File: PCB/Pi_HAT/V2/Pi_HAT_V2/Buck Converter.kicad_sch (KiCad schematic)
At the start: 19 parts, among them J5 XT60PW-M, J6 Conn_01x04_Male, U1 MP2315GJ-Z

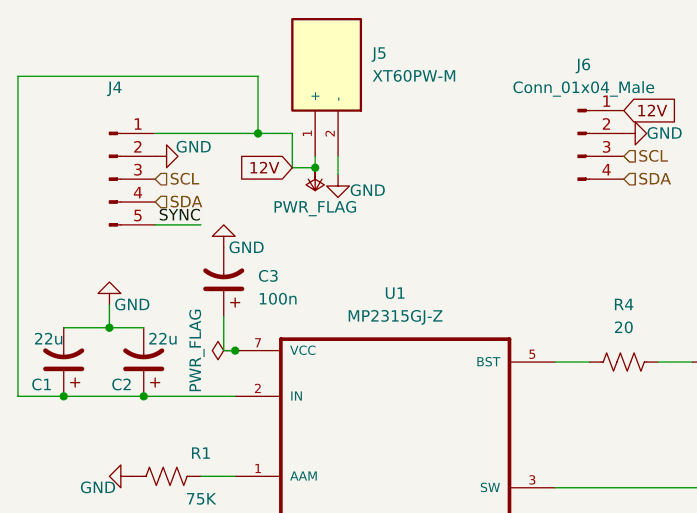
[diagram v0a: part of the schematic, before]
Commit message: Finished Buch .sch
Next need to start/finish the PCB traces
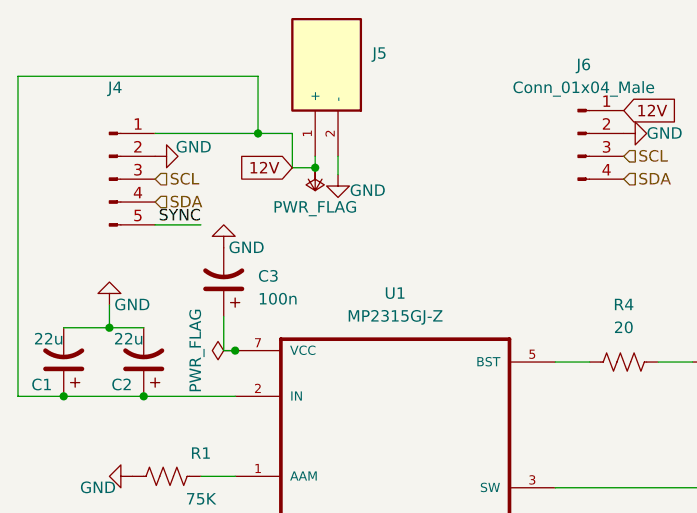
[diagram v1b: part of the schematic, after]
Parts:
- J5: value XT60PW-M -> (none); footprint .pretty:AMASS_XT60PW-M -> (none)
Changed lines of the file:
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@@
       (effects (font (size 1.27 1.27)) (justify right))
     )
-    (property "Value" "XT60PW-M" (id 1) (at 123.19 35.5599 90)
-      (effects (font (size 1.27 1.27)) (justify right))
-    )
-    (property "Footprint" ".pretty:AMASS_XT60PW-M" (id 2) (at 119.38 34.29 0)
+    (property "Value" "" (id 1) (at 123.19 35.5599 90)
+      (effects (font (size 1.27 1.27)) (justify right))
+    )
+    (property "Footprint" "" (id 2) (at 119.38 34.29 0)
       (effects (font (size 1.27 1.27)) (justify left bottom) hide)
     )
@@
       (effects (font (size 1.27 1.27)) hide)
     )
-    (property "Value" "" (id 1) (at 116.84 50.165 0))
+    (property "Value" "~" (id 1) (at 116.84 50.165 0))
     (property "Footprint" "" (id 2) (at 116.84 45.72 0)
       (effects (font (size 1.27 1.27)) hide)
@@
       (effects (font (size 1.27 1.27)) (justify left))
     )
-    (property "Value" "22u" (id 1) (at 101.6 64.77 0)
-      (effects (font (size 1.27 1.27)) (justify left))
-    )
+    (property "Value" "22u" (id 1) (at 97.79 64.77 0)
+      (effects (font (size 1.27 1.27)) (justify left))
+    )

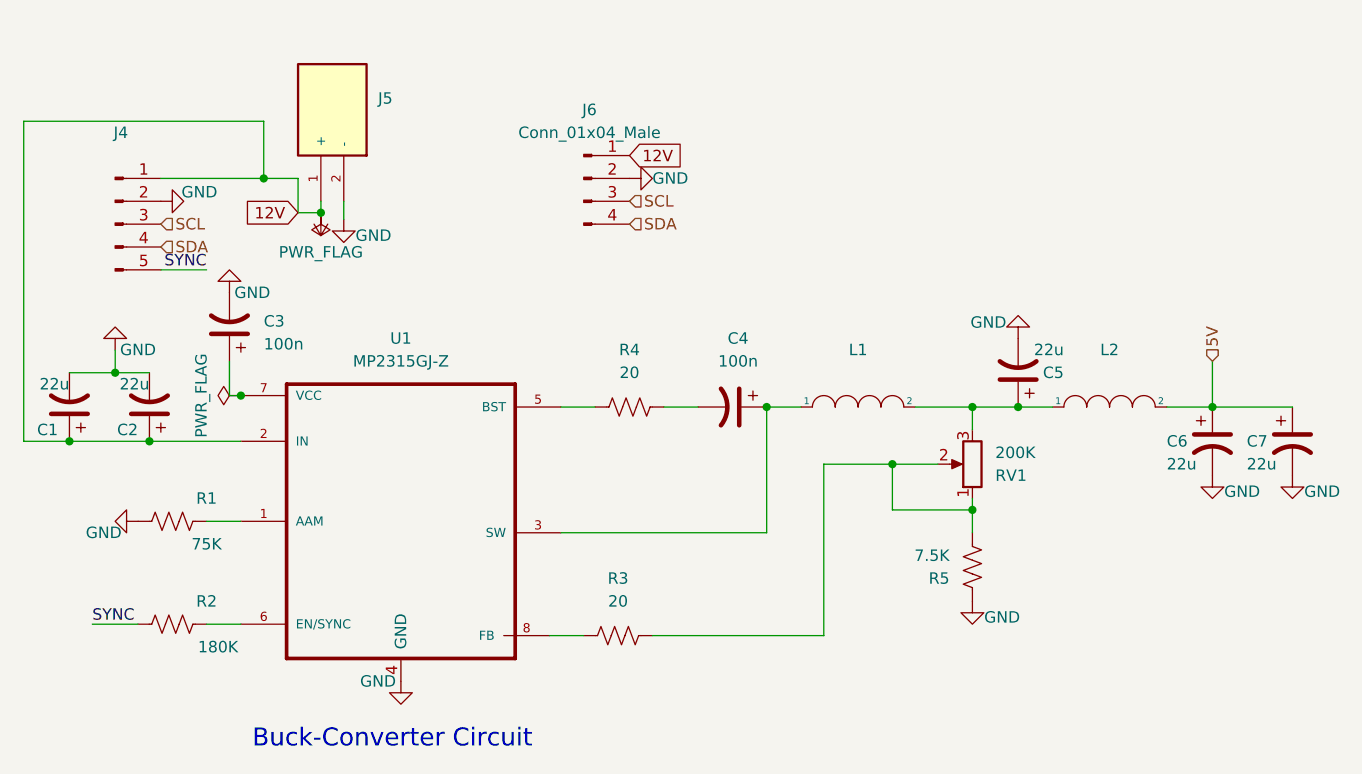
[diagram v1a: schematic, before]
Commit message: Updated
Added NANO_HAT and finished the PI_HAT V2 .sch, need to start/finish traces
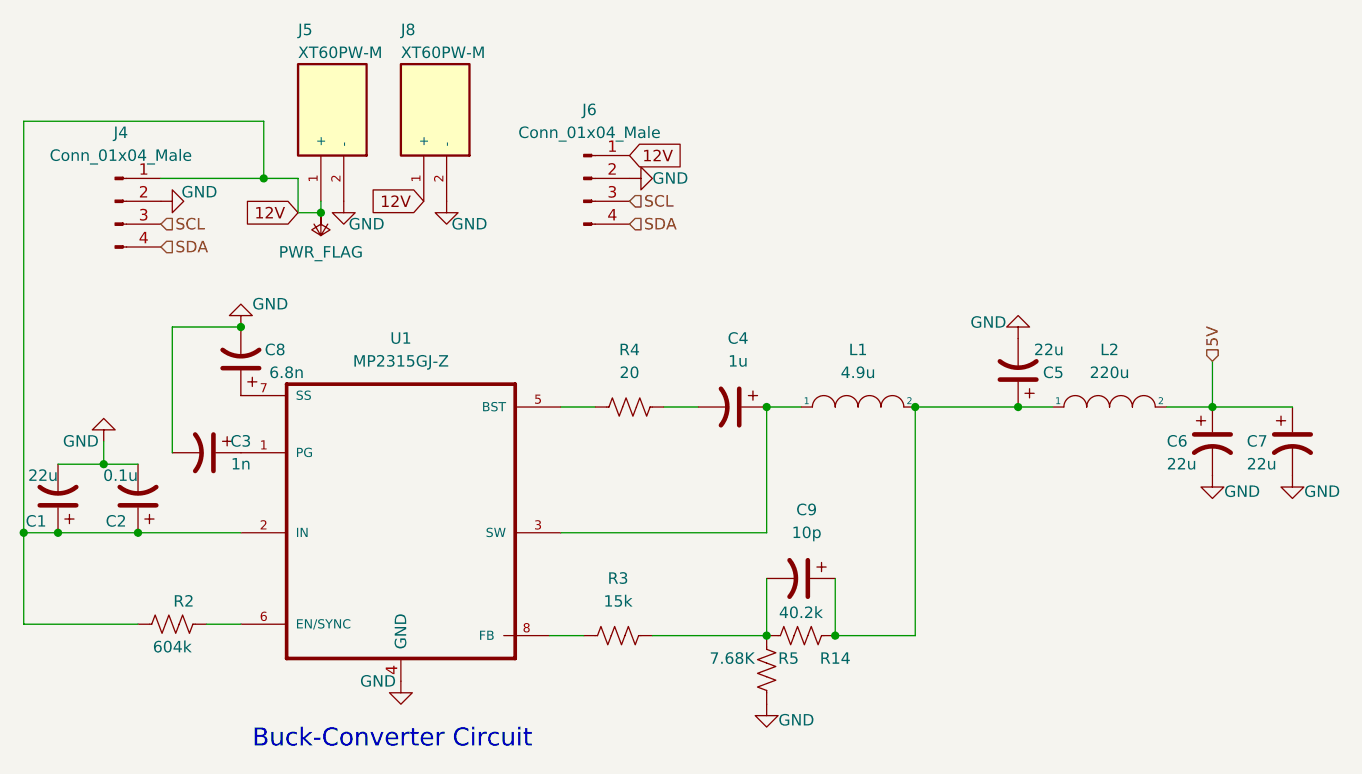
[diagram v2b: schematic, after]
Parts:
- removed J4: (no value), symbol Connector:Conn_01x05_Male
- removed R1: 75K, Resistor_SMD:R_0805_2012Metric_Pad1.20x1.40mm_HandSolder, symbol Device:R_US
- removed RV1: 200K, .pretty:TRIM_3296W-1-204LF, symbol Device:R_Potentiometer
- added C8: 6.8n, Capacitor_SMD:C_0603_1608Metric_Pad1.08x0.95mm_HandSolder, symbol Device:C_Polarized_US
- added C9: 10p, Capacitor_SMD:C_0603_1608Metric_Pad1.08x0.95mm_HandSolder, symbol Device:C_Polarized_US
- added J4: Conn_01x04_Male, Connector_PinHeader_2.54mm:PinHeader_1x04_P2.54mm_Vertical, symbol Connector:Conn_01x04_Male
- added J8: XT60PW-M, .pretty:AMASS_XT60PW-M, symbol XT60PW-M:XT60PW-M
- added R14: 40.2k, Resistor_SMD:R_0805_2012Metric_Pad1.20x1.40mm_HandSolder, symbol Device:R_US
- C2: value 22u -> 0.1u
- C3: value 100n -> 1n; footprint Capacitor_SMD:C_0805_2012Metric_Pad1.18x1.45mm_HandSolder -> Capacitor_SMD:C_0603_1608Metric_Pad1.08x0.95mm_HandSolder
- C4: value 100n -> 1u
- J5: value (none) -> XT60PW-M; footprint (none) -> .pretty:AMASS_XT60PW-M
- J6: footprint (none) -> Connector_PinHeader_2.54mm:PinHeader_1x04_P2.54mm_Vertical
- L1: value (none) -> 4.9u; footprint (none) -> .pretty:744777004; order https://www.digikey.com/en/products/detail/w%C3%BCrth-elekt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 -> https://www.mouser.com/ProductDetail/Coiltronics-Eaton/SD70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
- L2: value (none) -> 220u; footprint (none) -> .pretty:IND_AIRD-02-151K
- R2: value 180K -> 604k
- R3: value 20 -> 15k
- R4: footprint Resistor_SMD:R_0805_2012Metric_Pad1.20x1.40mm_HandSolder -> Resistor_SMD:R_0603_1608Metric_Pad0.98x0.95mm_HandSolder
- R5: value 7.5K -> 7.68K
- U1: footprint .pretty:SOT65P280X100-8N -> .pretty:MP2393GTL-P; Field4 Monolithic Power -> (none); Order (none) -> https://www.mouser.com/ProductDetail/Monolithic-Power-Syste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
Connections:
- net SYNC is gone; now on net +12V: R2.1
- net +12V: now also J4.1 (Pin_1), J8.1 (+)
- net GND: now also C8.2, J4.2 (Pin_2), J8.2 (-)
- net SCL: now also J4.3 (Pin_3)
- net SDA: now also J4.4 (Pin_4)
- net at U1.1 (PG): now also C3.1
- net at U1.7 (SS): now also C8.1; no longer C3.1
- net at R3.2, R5.2: now also C9.2, R14.2
- net at C5.1, L1.2, L2.1: now also C9.1, R14.1
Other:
- moved on the sheet: C1, C2, C3, R5

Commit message: Updated (Gerber)
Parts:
- removed J8: XT60PW-M, .pretty:AMASS_XT60PW-M, symbol XT60PW-M:XT60PW-M
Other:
- moved on the sheet: J6
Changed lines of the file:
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@@
     )
   )
-  (global_label "12V" (shape input) (at 128.27 44.45 180) (fields_autoplaced)
-    (effects (font (size 1.27 1.27)) (justify right))
-    (property "Intersheet References" "${INTERSHEET_REFS}" (id 0) (at 4.318 -2.032 0)
-      (effects (font (size 1.27 1.27)) hide)
-    )
-  )
-  (global_label "12V" (shape input) (at 151.13 39.37 0) (fields_autoplaced)
-    (effects (font (size 1.27 1.27)) (justify left))
-    (property "Intersheet References" "${INTERSHEET_REFS}" (id 0) (at 275.082 85.852 0)
-      (effects (font (size 1.27 1.27)) hide)
-    )
-  )
-  (hierarchical_label "SCL" (shape input) (at 151.13 44.45 0)
+  (global_label "12V" (shape input) (at 137.16 34.544 0) (fields_autoplaced)
+    (effects (font (size 1.27 1.27)) (justify left))
+    (property "Intersheet References" "${INTERSHEET_REFS}" (id 0) (at 261.112 81.026 0)
+      (effects (font (size 1.27 1.27)) hide)
+    )
+  )
+  (hierarchical_label "SCL" (shape input) (at 137.16 39.624 0)
     (effects (font (size 1.27 1.27)) (justify left))
   )
@@
     (effects (font (size 1.27 1.27)) (justify left))
   )
-  (hierarchical_label "SDA" (shape input) (at 151.13 46.99 0)
+  (hierarchical_label "SDA" (shape input) (at 137.16 42.164 0)
     (effects (font (size 1.27 1.27)) (justify left))
   )
@@
     (property "Datasheet" "~" (id 3) (at 224.79 71.12 0)
       (effects (font (size 1.27 1.27)) hide)
-    )
-    (pin "1")
-    (pin "2")
-  )
-  (symbol (lib_id "XT60PW-M:XT60PW-M") (at 130.81 34.29 90) (unit 1)
-    (in_bom yes) (on_board yes)
-    (property "Reference" "J8" (id 0) (at 125.73 25.4 90)
-      (effects (font (size 1.27 1.27)) (justify right))
-    )
-    (property "Value" "XT60PW-M" (id 1) (at 125.73 27.94 90)
-      (effects (font (size 1.27 1.27)) (justify right))
-    )
-    (property "Footprint" ".pretty:AMASS_XT60PW-M" (id 2) (at 130.81 34.29 0)
-      (effects (font (size 1.27 1.27)) (justify left bottom) hide)
-    )
-    (property "Datasheet" "" (id 3) (at 130.81 34.29 0)
-      (effects (font (size 1.27 1.27)) (justify left bottom) hide)
-    )
-    (property "STANDARD" "Manufacturer recommendations" (id 4) (at 130.81 34.29 0)
-      (effects (font (size 1.27 1.27)) (justify left bottom) hide)
-    )
-    (property "PARTREV" "V1.2" (id 5) (at 130.81 34.29 0)
-      (effects (font (size 1.27 1.27)) (justify left bottom) hide)
-    )
-    (property "MANUFACTURER" "AMASS" (id 6) (at 130.81 34.29 0)
-      (effects (font (size 1.27 1.27)) (justify left bottom) hide)
-    )
-    (property "MAXIMUM_PACKAGE_HEIGHT" "8.4 mm" (id 7) (at 130.81 34.29 0)
-      (effects (font (size 1.27 1.27)) (justify left bottom) hide)
     )
     (pin "1")
@@
     (pin "1")
     (pin "2")
-  )
-  (symbol (lib_id "power:GND") (at 130.81 44.45 0) (unit 1)
-    (in_bom yes) (on_board yes)
-    (property "Reference" "#PWR0116" (id 0) (at 130.81 50.8 0)
-      (effects (font (size 1.27 1.27)) hide)
-    )
-    (property "Value" "GND" (id 1) (at 133.35 46.99 0))
-    (property "Footprint" "" (id 2) (at 130.81 44.45 0)
-      (effects (font (size 1.27 1.27)) hide)
-    )
-    (property "Datasheet" "" (id 3) (at 130.81 44.45 0)
-      (effects (font (size 1.27 1.27)) hide)
-    )
-    (pin "1")
   )
   (symbol (lib_id "Device:R_US") (at 151.13 67.31 90) (unit 1)
@@
     (pin "2")
   )
-  (symbol (lib_id "power:GND") (at 151.13 41.91 90) (unit 1)
-    (in_bom yes) (on_board yes)
-    (property "Reference" "#PWR0117" (id 0) (at 157.48 41.91 0)
-      (effects (font (size 1.27 1.27)) hide)
-    )
-    (property "Value" "GND" (id 1) (at 153.67 41.91 90)
-      (effects (font (size 1.27 1.27)) (justify right))
-    )
-    (property "Footprint" "" (id 2) (at 151.13 41.91 0)
-      (effects (font (size 1.27 1.27)) hide)
-    )
-    (property "Datasheet" "" (id 3) (at 151.13 41.91 0)
+  (symbol (lib_id "power:GND") (at 137.16 37.084 90) (unit 1)
+    (in_bom yes) (on_board yes)
+    (property "Reference" "#PWR0117" (id 0) (at 143.51 37.084 0)
+      (effects (font (size 1.27 1.27)) hide)
+    )
+    (property "Value" "GND" (id 1) (at 139.7 37.084 90)
+      (effects (font (size 1.27 1.27)) (justify right))
+    )
+    (property "Footprint" "" (id 2) (at 137.16 37.084 0)
+      (effects (font (size 1.27 1.27)) hide)
+    )
+    (property "Datasheet" "" (id 3) (at 137.16 37.084 0)
       (effects (font (size 1.27 1.27)) hide)
     )
@@
     (pin "2")
   )
-  (symbol (lib_id "Connector:Conn_01x04_Male") (at 146.05 41.91 0) (unit 1)
-    (in_bom yes) (on_board yes) (fields_autoplaced)
-    (property "Reference" "J6" (id 0) (at 146.685 34.29 0))
-    (property "Value" "Conn_01x04_Male" (id 1) (at 146.685 36.83 0))
-    (property "Footprint" "Connector_PinHeader_2.54mm:PinHeader_1x04_P2.54mm_Vertical" (id 2) (at 146.05 41.91 0)
-      (effects (font (size 1.27 1.27)) hide)
-    )
-    (property "Datasheet" "~" (id 3) (at 146.05 41.91 0)
-      (effects (font (size 1.27 1.27)) hide)
-    )
+  (symbol (lib_id "Connector:Conn_01x04_Male") (at 132.08 37.084 0) (unit 1)
+    (in_bom yes) (on_board yes) (fields_autoplaced)
+    (property "Reference" "J6" (id 0) (at 132.715 29.464 0))
+    (property "Value" "Conn_01x04_Male" (id 1) (at 132.715 32.004 0))
+    (property "Footprint" "Connector_PinHeader_2.54mm:PinHeader_1x04_P2.54mm_Vertical" (id 2) (at 132.08 37.084 0)
+      (effects (font (size 1.27 1.27)) hide)
+    )
+    (property "Datasheet" "~" (id 3) (at 132.08 37.084 0)
+      (effects (font (size 1.27 1.27)) hide)
+    )
